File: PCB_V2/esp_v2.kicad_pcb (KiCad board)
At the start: 2 copper layers, 86 x 67.5 mm, 13 parts, among them J2 Conn_01x03_Socket, J3 Screw_Terminal_01x02, U1 ESP-32S

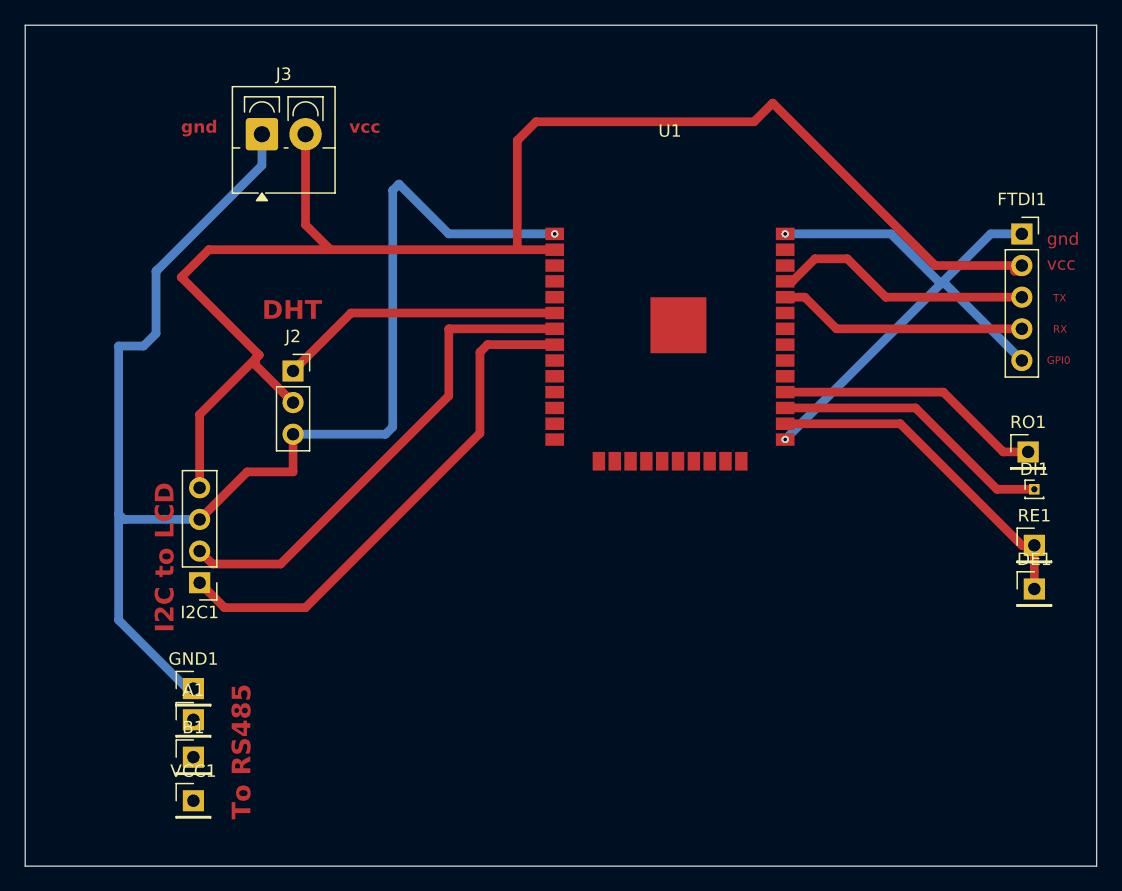
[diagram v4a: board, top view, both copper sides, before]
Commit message: correction on I2C for the lcd
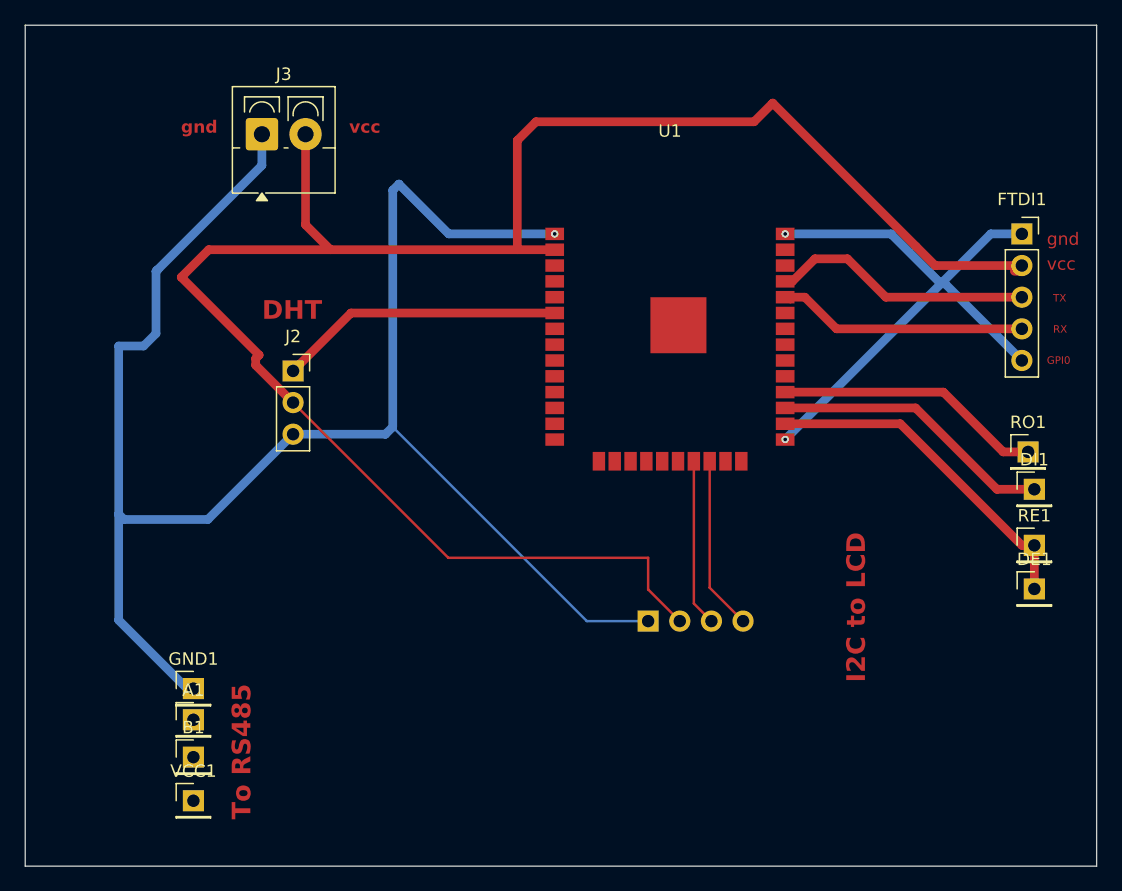
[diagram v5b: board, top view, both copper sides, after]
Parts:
- DI1: footprint Connector_PinHeader_1.00mm:PinHeader_1x01_P1.00mm_Vertical -> Connector_PinHeader_2.54mm:PinHeader_1x01_P2.54mm_Vertical
- I2C1: moved to B.Cu
- moved I2C1 36.1 mm to (115.0, 105.1), turned to -90 degrees
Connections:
- I2C1 pad 1: Net-(I2C1-Pin_1) -> GND
- I2C1 pad 2: Net-(I2C1-Pin_2) -> VCC
- I2C1 pad 3: GND -> Net-(I2C1-Pin_3)
- I2C1 pad 4: VCC -> Net-(I2C1-Pin_4)
- U1 pad 21: unconnected-(U1-SD0-Pad21) -> Net-(I2C1-Pin_3)
- U1 pad 22: unconnected-(U1-SD1-Pad22) -> Net-(I2C1-Pin_4)
- U1 pad 7: Net-(I2C1-Pin_2) -> unconnected-(U1-IO35-Pad7)
- U1 pad 8: Net-(I2C1-Pin_1) -> unconnected-(U1-IO32-Pad8)
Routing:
- net Net-(I2C1-Pin_1): track 42.5 -> 0.00 mm
- net Net-(I2C1-Pin_2): track 39.9 -> 0.00 mm
- net VCC: track 124.1 -> 151.3 mm
- net GND: track 114.3 -> 139.5 mm
- net Net-(I2C1-Pin_4): track 0.00 -> 13.9 mm
- net Net-(I2C1-Pin_3): track 0.00 -> 13.4 mm
